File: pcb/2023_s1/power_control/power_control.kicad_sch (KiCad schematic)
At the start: 26 parts, among them J1 Conn_01x05_Male, Q1 TIP122, Q2 TIP122, U1 40106, U2 4N25, U3 4N25

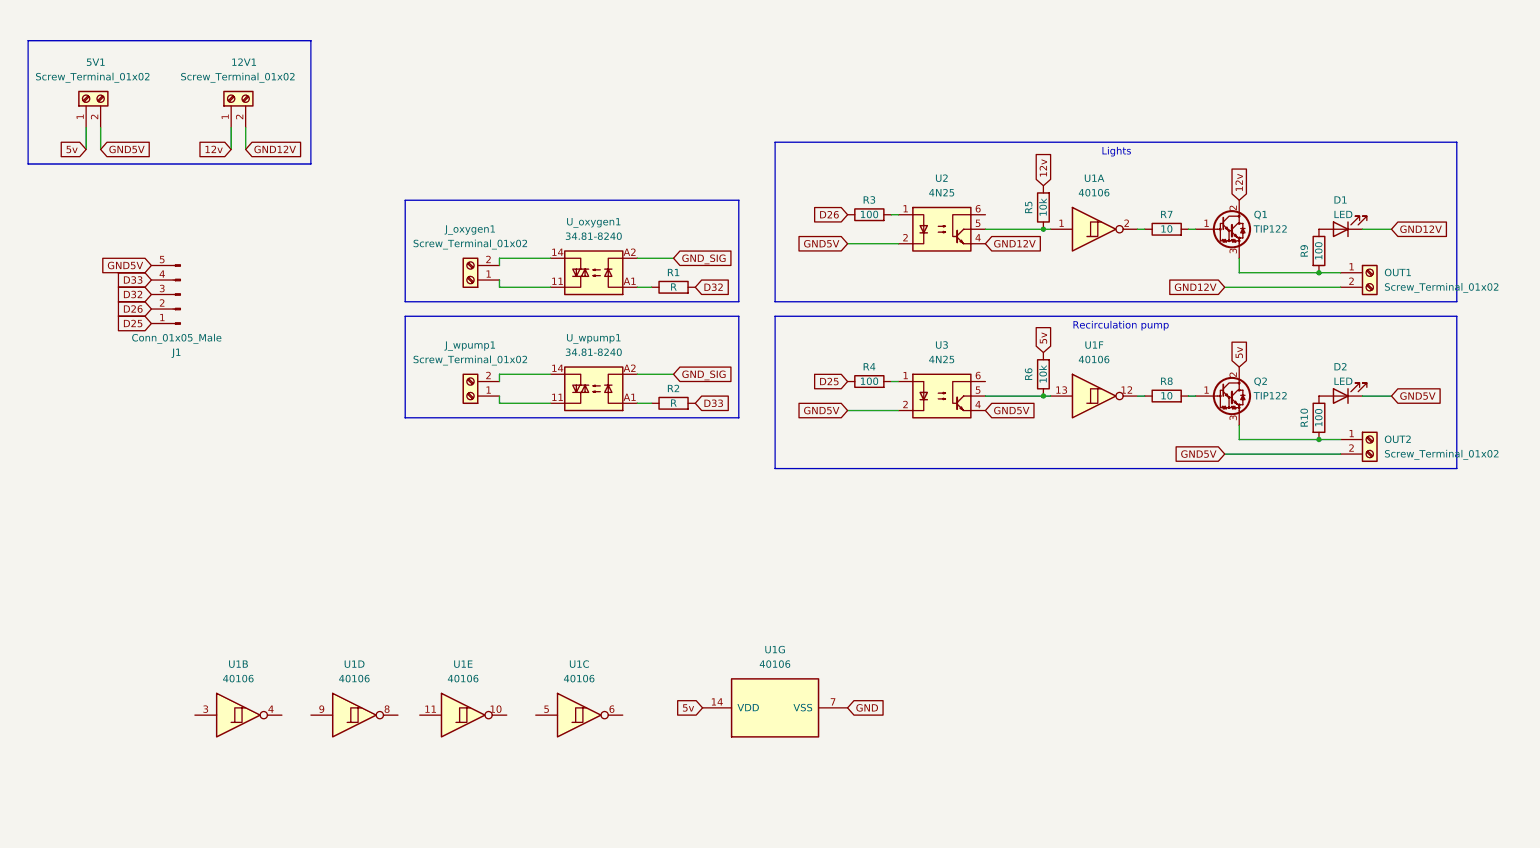
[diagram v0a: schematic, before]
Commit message: corrected power control pcb, and repositioned most of the elements
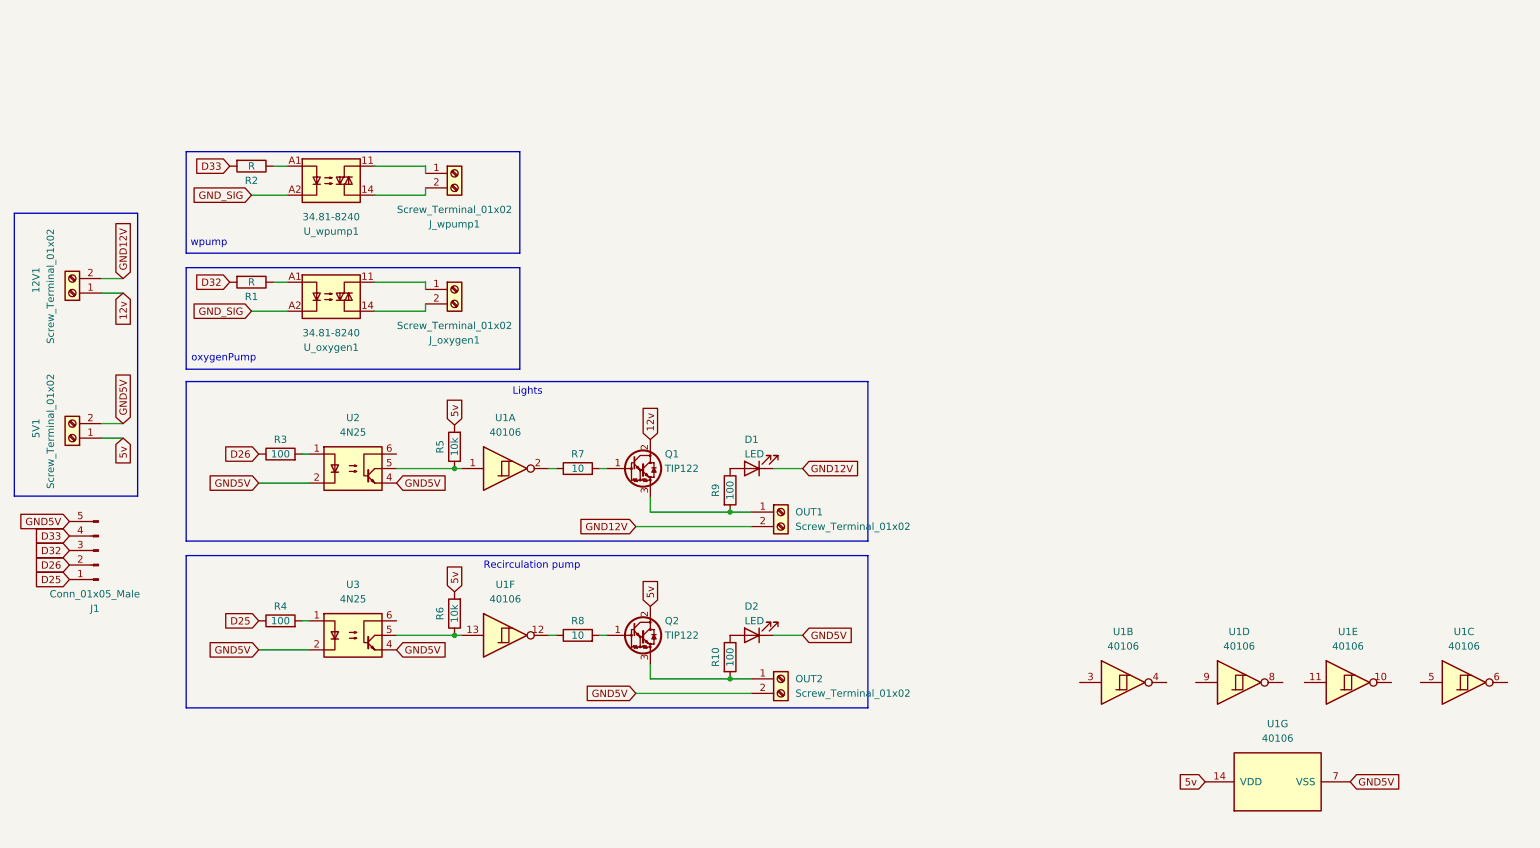
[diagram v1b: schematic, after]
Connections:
- net GND is gone; now on net GND5V: U1.7 (VSS)
- net 12v: no longer R5.2
- net 5v: now also R5.2
- net GND12V: no longer U2.4
- net GND5V: now also U2.4
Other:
- note added: "oxygenPump"
- note added: "wpump"
- moved on the sheet: 12V1, 5V1, D1, D2, J1, J_oxygen1, J_wpump1, OUT1, OUT2, Q1, Q2, R1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

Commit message: update, finished connecting the power pcb module, and added the fan control to both pcbs
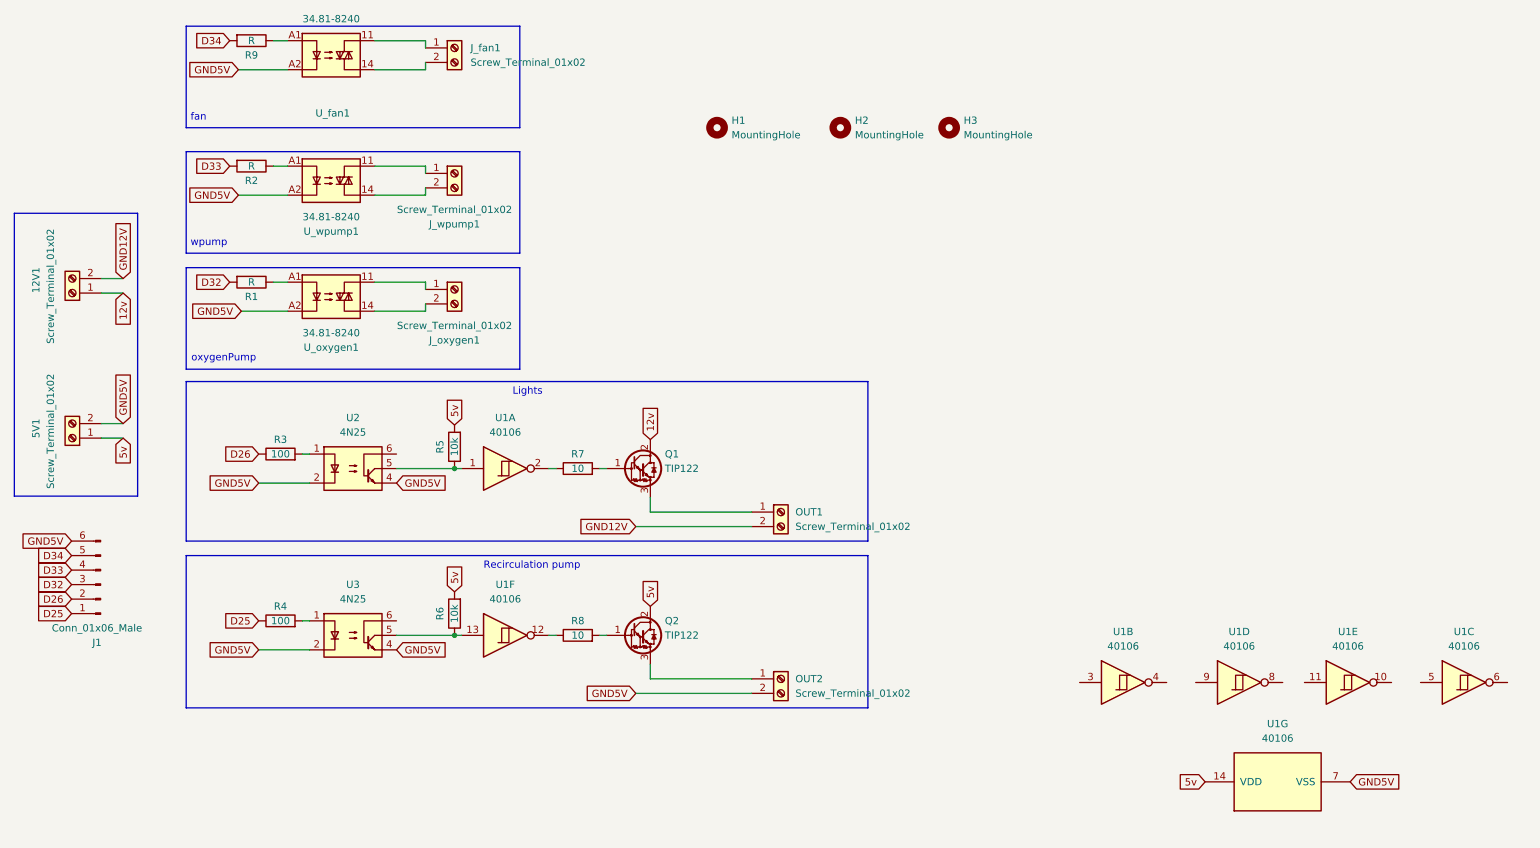
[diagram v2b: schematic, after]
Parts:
- removed D1, D2: LED, LED_THT:LED_D3.0mm_Clear, symbol Device:LED
- removed J1: Conn_01x05_Male, Connector_JST:JST_EH_B5B-EH-A_1x05_P2.50mm_Vertical, symbol Connector:Conn_01x05_Male
- removed R10: 100, Resistor_THT:R_Axial_DIN0204_L3.6mm_D1.6mm_P2.54mm_Vertical, symbol Device:R
- added H1, H2, H3: MountingHole, MountingHole:MountingHole_3.2mm_M3_DIN965_Pad, symbol Mechanical:MountingHole
- added J1: Conn_01x06_Male, Connector_JST:JST_EH_B6B-EH-A_1x06_P2.50mm_Vertical, symbol Connector:Conn_01x06_Male
- added J_fan1: Screw_Terminal_01x02, TerminalBlock:TerminalBlock_Altech_AK300-2_P5.00mm, symbol Connector:Screw_Terminal_01x02
- added U_fan1: 34.81-8240, OptoDevice:Finder_34.81, symbol Relay_SolidState:34.81-8240
- R9: value 100 -> R; footprint Resistor_THT:R_Axial_DIN0204_L3.6mm_D1.6mm_P2.54mm_Vertical -> Resistor_THT:R_Axial_DIN0204_L3.6mm_D1.6mm_P5.08mm_Vertical
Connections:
- net GND_SIG is gone; now on net GND5V: U_oxygen1.A2, U_wpump1.A2
- net D25: now also J1.1 (Pin_1)
- net D26: now also J1.2 (Pin_2)
- net D32: now also J1.3 (Pin_3)
- net D33: now also J1.4 (Pin_4)
- net GND5V: now also J1.6 (Pin_6), U_fan1.A2
- net at R9.1: now also U_fan1.A1
- net at OUT1.1 (Pin_1), Q1.3 (E): no longer R9.2
- new net: J_fan1.1 (Pin_1), U_fan1.11
- new net: J_fan1.2 (Pin_2), U_fan1.14
- new net D34: J1.5 (Pin_5), R9.2
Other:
- note added: "fan"

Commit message: fix, separated the light control into another pcb, due to the different voltage it handles and confort for the use
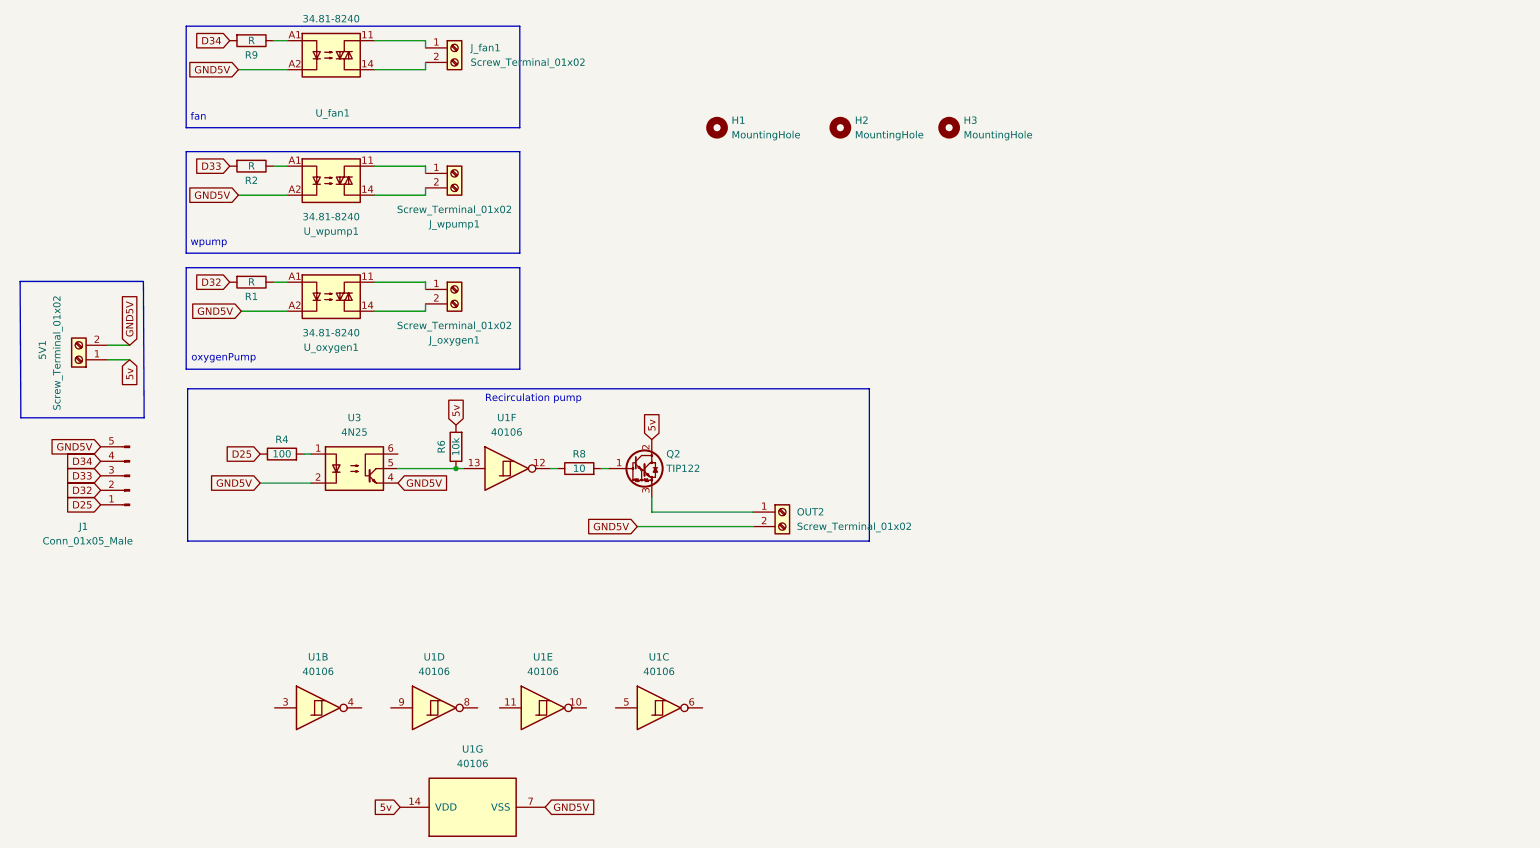
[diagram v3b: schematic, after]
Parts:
- removed 12V1, OUT1: Screw_Terminal_01x02, TerminalBlock:TerminalBlock_Altech_AK300-2_P5.00mm, symbol Connector:Screw_Terminal_01x02
- removed J1: Conn_01x06_Male, Connector_JST:JST_EH_B6B-EH-A_1x06_P2.50mm_Vertical, symbol Connector:Conn_01x06_Male
- removed Q1: TIP122, Package_TO_SOT_THT:TO-220-3_Vertical, symbol Transistor_BJT:TIP122
- removed R3: 100, Resistor_THT:R_Axial_DIN0204_L3.6mm_D1.6mm_P2.54mm_Vertical, symbol Device:R
- removed R5: 10k, Resistor_THT:R_Axial_DIN0204_L3.6mm_D1.6mm_P2.54mm_Vertical, symbol Device:R
- removed R7: 10, Resistor_THT:R_Axial_DIN0204_L3.6mm_D1.6mm_P2.54mm_Vertical, symbol Device:R
- removed unit 1 of U1
- removed U2: 4N25, Package_DIP:DIP-6_W7.62mm, symbol Isolator:4N25
- added J1: Conn_01x05_Male, Connector_JST:JST_EH_B5B-EH-A_1x05_P2.50mm_Vertical, symbol Connector:Conn_01x05_Male
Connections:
- net D25: now also J1.1 (Pin_1)
- net D32: now also J1.2 (Pin_2)
- net D33: now also J1.3 (Pin_3)
- net D34: now also J1.4 (Pin_4)
- net GND5V: now also J1.5 (Pin_5)
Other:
- note removed: "Lights"
- moved on the sheet: 5V1, OUT2, Q2, R4, R6, R8, U1B, U1C, U1D, U1E, U1F, U1G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
